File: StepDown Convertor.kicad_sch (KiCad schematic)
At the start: 7 parts, among them U9 LMR14203

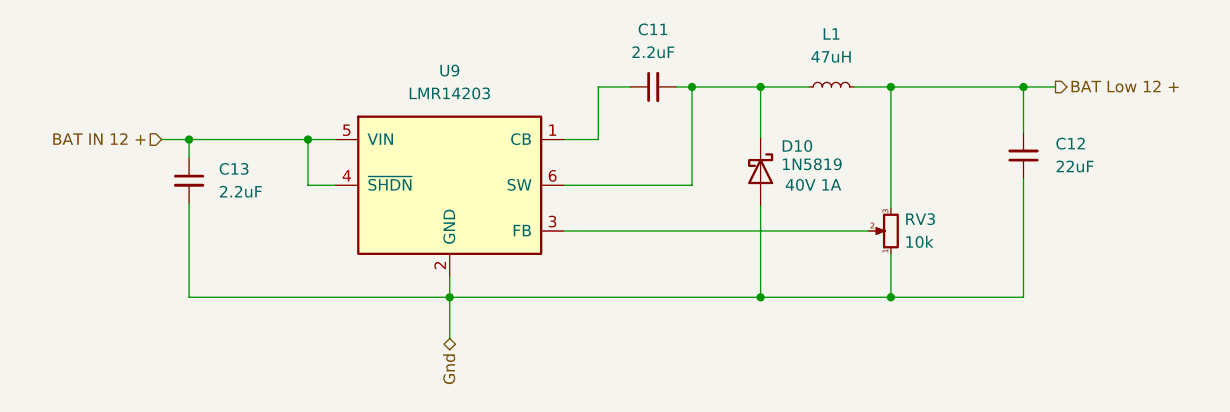
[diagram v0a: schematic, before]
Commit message: Fix comparator out signal pullup
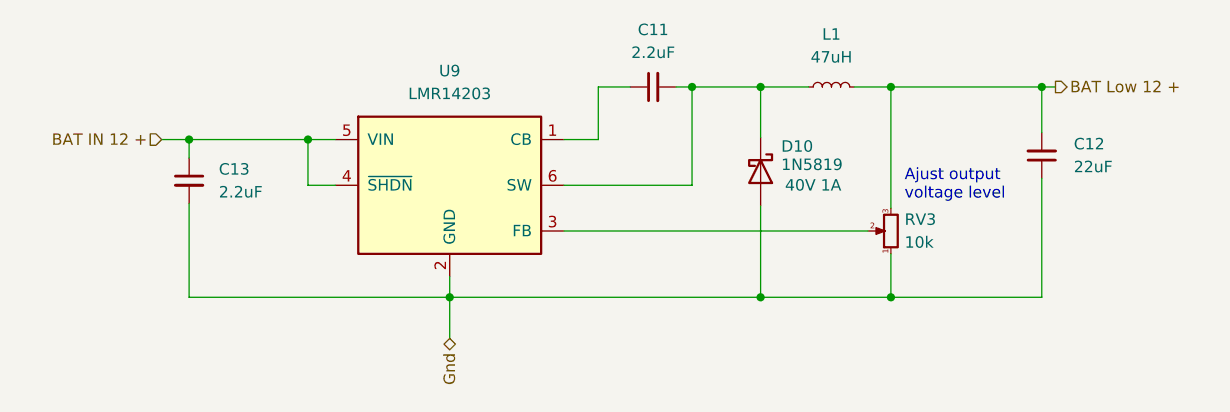
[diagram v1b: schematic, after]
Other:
- note added: "Ajust output voltage level"
- moved on the sheet: C12
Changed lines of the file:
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@@
 	(generator_version "9.0")
 	(paper "A4")
+	(text "Ajust output \nvoltage level "
+		(exclude_from_sim no)
+		(at 180.848 105.41 0)
+		(effects
+			(font
+				(size 1.27 1.27)
+			)
+			(justify left)
+		)
+	)
 	(junction
 		(at 164.846 117.856)
@@
 	)
 	(junction
-		(at 194.056 94.488)
+		(at 196.088 94.488)
 		(diameter 0)
 		(color 0 0 0 0)
@@
 	(wire
 		(pts
-			(xy 194.056 104.648) (xy 194.056 117.856)
+			(xy 196.088 104.648) (xy 196.088 117.856)
 		)
 		(stroke
@@
 	(wire
 		(pts
-			(xy 194.056 94.488) (xy 197.612 94.488)
-		)
-		(stroke
-			(width 0)
-			(type default)
-		)
-	)
-	(wire
-		(pts
 			(xy 157.226 94.488) (xy 164.846 94.488)
 		)
@@
 	(wire
 		(pts
+			(xy 196.088 94.488) (xy 197.612 94.488)
+		)
+		(stroke
+			(width 0)
+			(type default)
+		)
+	)
+	(wire
+		(pts
 			(xy 179.324 117.856) (xy 164.846 117.856)
 		)
@@
 	(wire
 		(pts
-			(xy 179.324 94.488) (xy 194.056 94.488)
+			(xy 179.324 94.488) (xy 196.088 94.488)
 		)
 		(stroke
@@
 	(wire
 		(pts
-			(xy 179.324 117.856) (xy 194.056 117.856)
-		)
-		(stroke
-			(width 0)
-			(type default)
-		)
-	)
-	(wire
-		(pts
-			(xy 194.056 99.568) (xy 194.056 94.488)
+			(xy 179.324 117.856) (xy 196.088 117.856)
+		)
+		(stroke
+			(width 0)
+			(type default)
+		)
+	)
+	(wire
+		(pts
+			(xy 196.088 99.568) (xy 196.088 94.488)
 		)
 		(stroke
@@
 	(symbol
 		(lib_id "Device:C_Small")
-		(at 194.056 102.108 180)
+		(at 196.088 102.108 180)
 		(unit 1)
 		(exclude_from_sim no)
@@
 		(fields_autoplaced yes)
 		(property "Reference" "C12"
-			(at 197.612 100.8315 0)
+			(at 199.644 100.8315 0)
 			(effects
 				(font
@@
 		)
 		(property "Value" "22uF"
-			(at 197.612 103.3715 0)
+			(at 199.644 103.3715 0)
 			(effects
 				(font
@@
 		)
 		(property "Footprint" "Capacitor_SMD:C_1210_3225Metric_Pad1.33x2.70mm_HandSolder"
-			(at 194.056 102.108 0)
+			(at 196.088 102.108 0)
 			(effects
 				(font
@@
 		)
 		(property "Datasheet" "~"
-			(at 194.056 102.108 0)
+			(at 196.088 102.108 0)
 			(effects
 				(font
@@
 		)
 		(property "Description" "Unpolarized capacitor, small symbol"
-			(at 194.056 102.108 0)
+			(at 196.088 102.108 0)
 			(effects
 				(font
@@
 		)
 		(property "descr" ""
-			(at 194.056 102.108 0)
-			(effects
-				(font
+			(at 196.088 102.108 0)
+			(effects
+				(font
